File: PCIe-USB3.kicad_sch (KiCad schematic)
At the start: 55 parts, among them J12 USB3_A, J14 Conn_02x05_Odd_Even, Q2 DMG1012T, U10 VL805, U6 AP3429KTTR-G1, U7 AP22653W6, Y1 25MHz

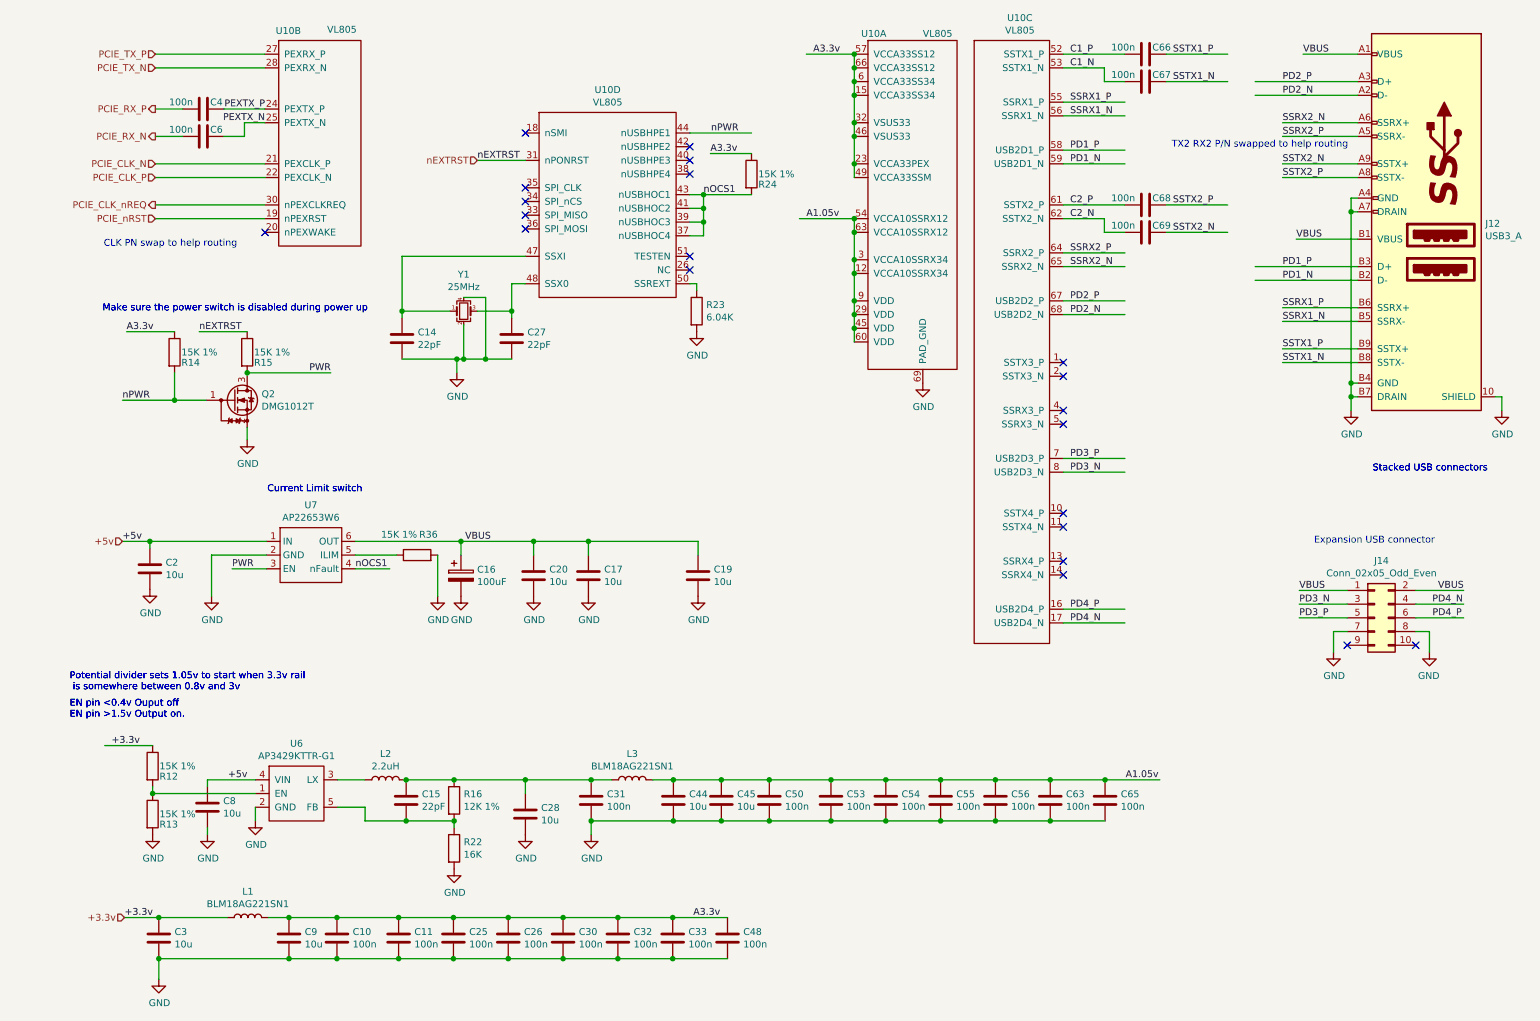
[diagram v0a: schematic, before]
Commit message: Removing unneeded items
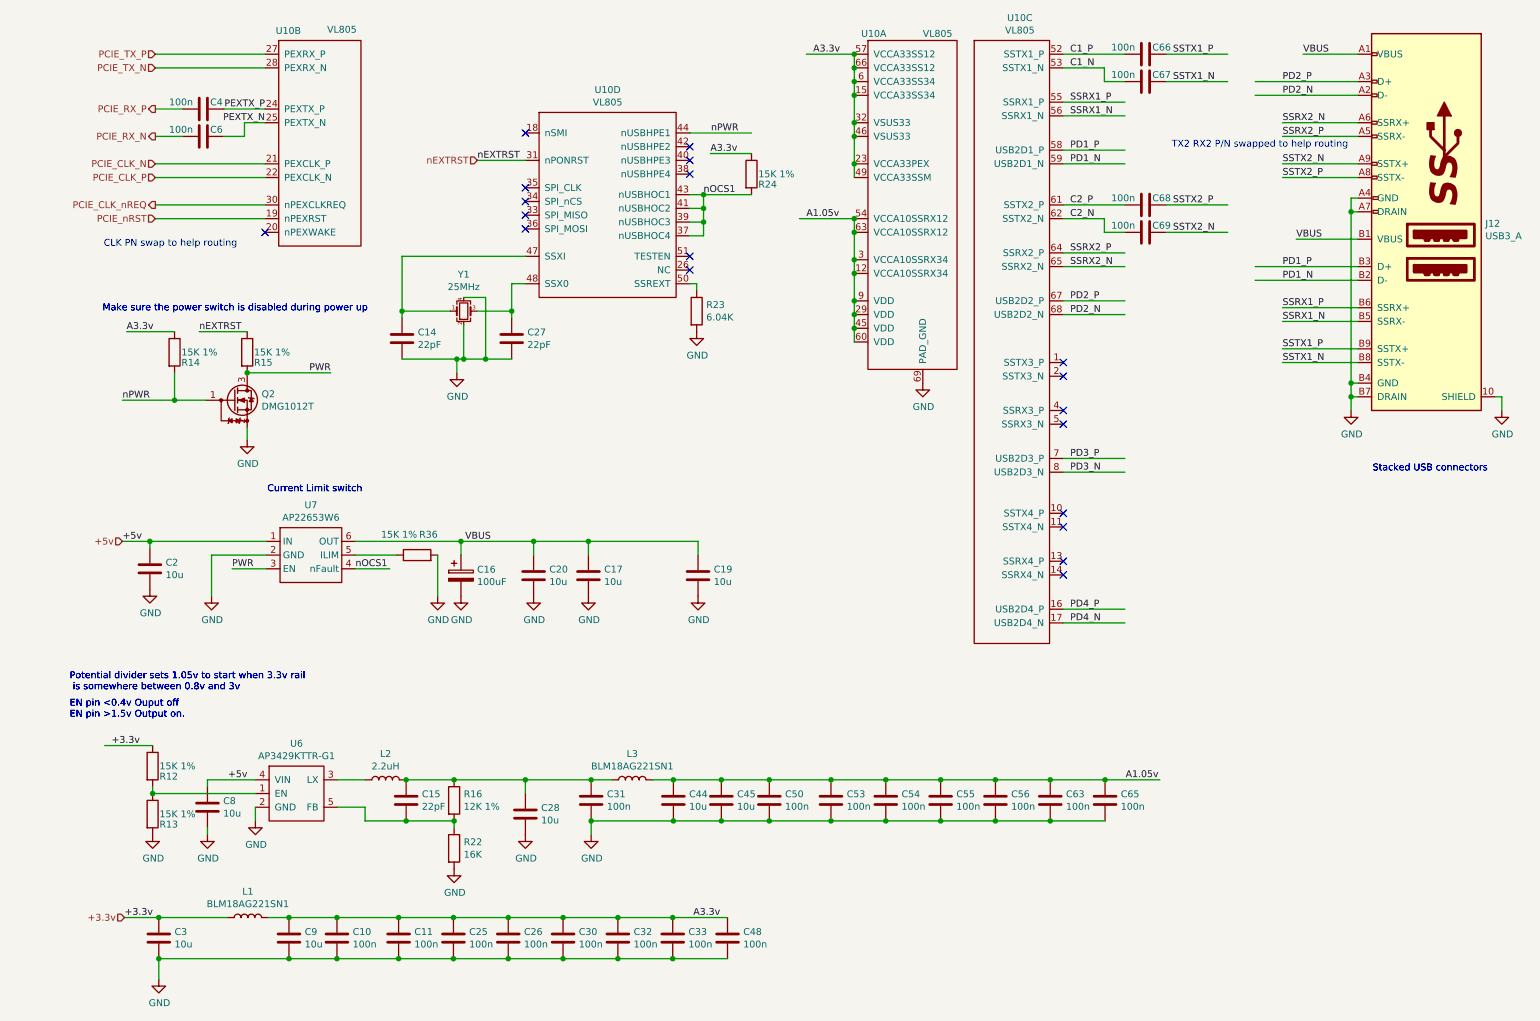
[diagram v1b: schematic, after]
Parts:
- removed J14: Conn_02x05_Odd_Even, Connector_PinHeader_2.54mm:PinHeader_2x05_P2.54mm_Vertical, symbol Connector_Generic:Conn_02x05_Odd_Even
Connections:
- no-connect marks 21 -> 19
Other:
- note removed: "Expansion USB connector"
